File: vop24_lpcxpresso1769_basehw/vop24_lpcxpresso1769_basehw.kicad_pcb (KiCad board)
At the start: 2 copper layers, 113 parts, among them J1 Micro_SD_Card, J101 Conn_01x03_Male, J201 Screw_Terminal_01x02, J301 USB_B_Micro, J302 Conn_01x06_Male, J303 Conn_01x05_Male, J304 Screw_Terminal_01x02, J401 Conn_01x02, J402 Conn_01x02, J403 Conn_01x02, J404 Conn_01x04, J405 Conn_01x04, J406 Conn_01x04, U1 LPCXpresso1769, U101 MCP1700T-3302E_TT, U102 MCP1700T-3302E_TT, U103 TPS63001, U201 LM358, U301 TPD4S014, U302 LTC4411, U303 LT1512, U401 ADS1292, U402 LM334, U403 LM334, U404 LM334

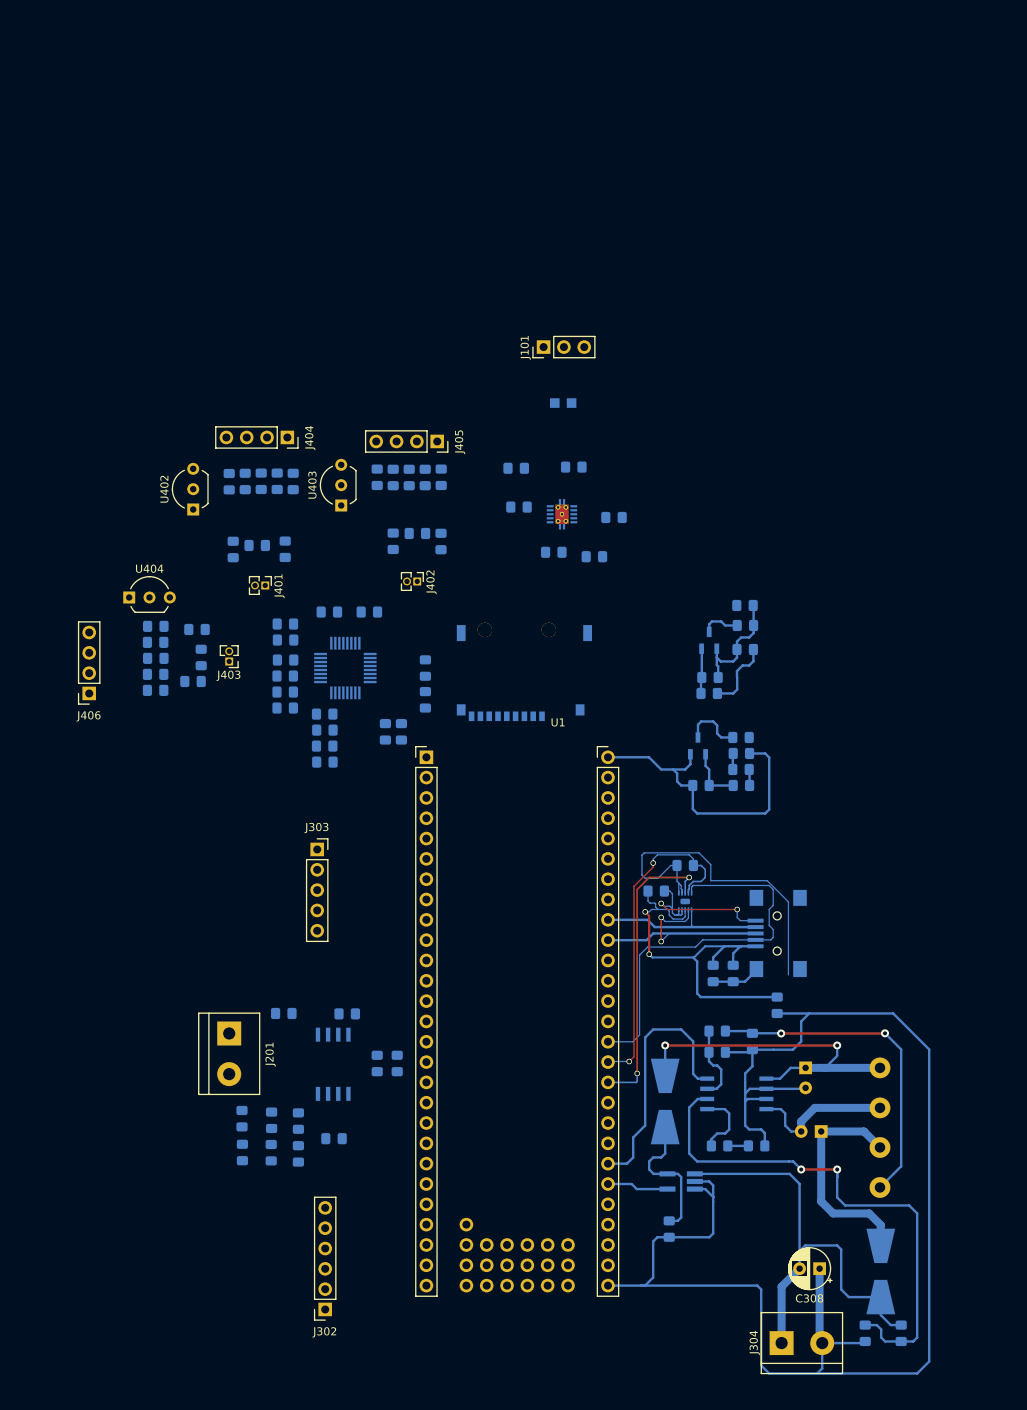
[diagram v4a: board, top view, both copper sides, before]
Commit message: PCB: ruteo de fuentes.    SCH: separacion de pistas de masa en fuentes
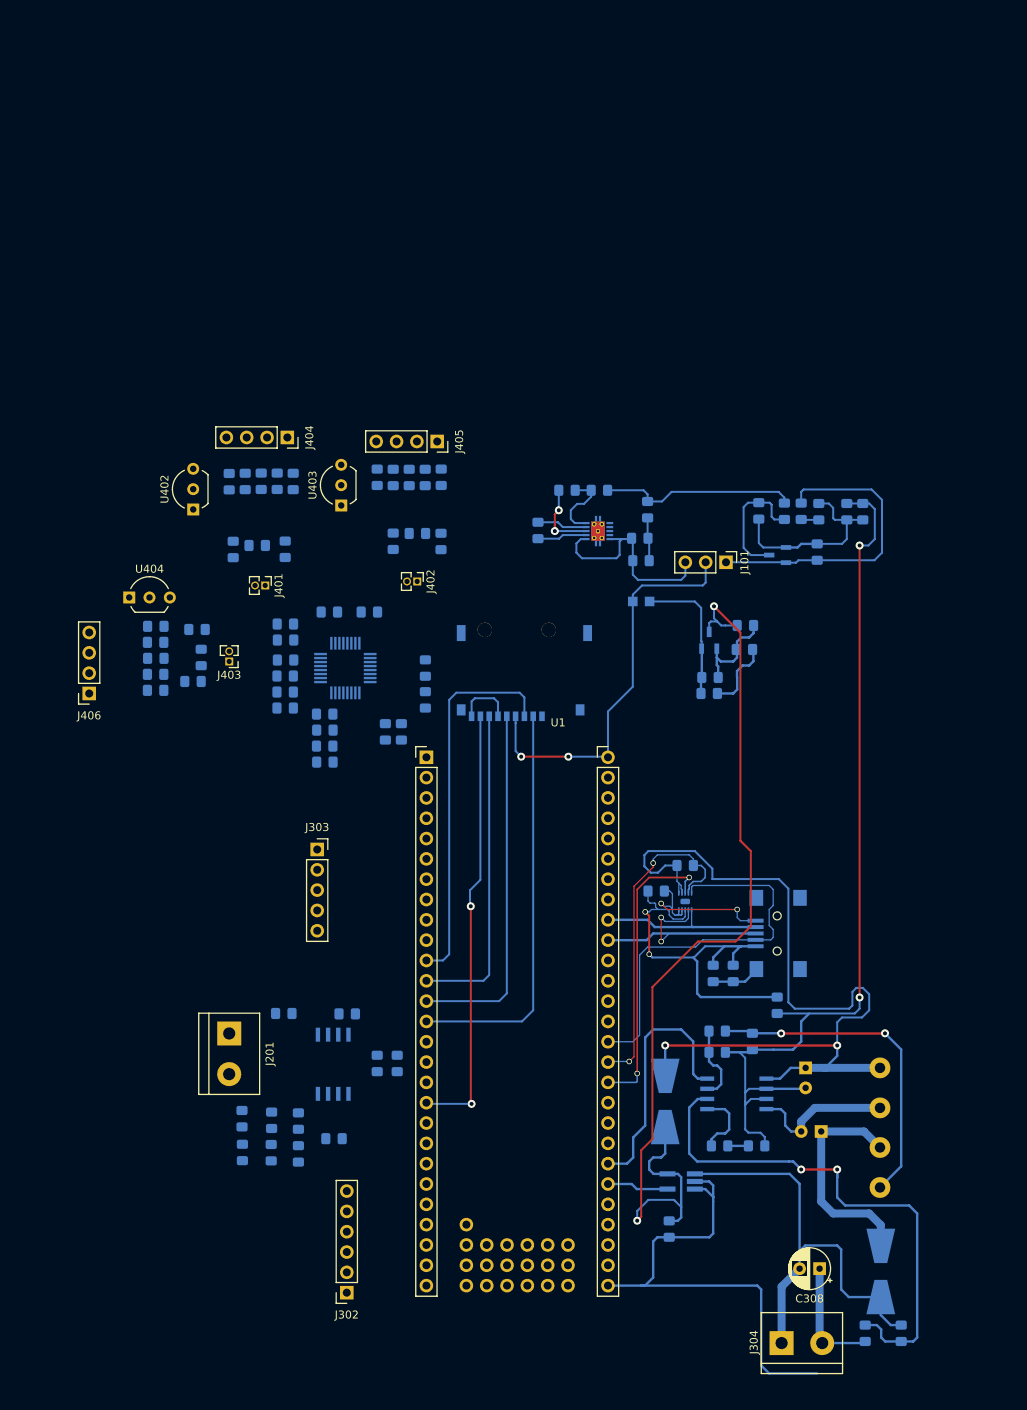
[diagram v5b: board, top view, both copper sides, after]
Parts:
- added R106: 1k, Resistor_SMD:R_0805_2012Metric_Pad1.15x1.40mm_HandSolder, B.Cu at (119.4, 92.0)
- R103: value 100 -> 0
- R104: value 1k -> 100
- moved R101 36.7 mm to (132.2, 74.8), turned to 90 degrees
- moved J101 35.3 mm to (117.1, 81.1), turned to 270 degrees
- moved R104 32.7 mm to (124.4, 74.7), turned to 90 degrees
- moved C105 32.6 mm to (128.5, 79.8), turned to 90 degrees
- moved D101 31.2 mm to (126.5, 74.7), turned to 90 degrees
- moved C101 28.4 mm to (121.2, 74.7), turned to 270 degrees
- moved FB101 26.6 mm to (106.5, 86.0), turned to 180 degrees
- moved U102 25.8 mm to (123.5, 80.2), turned to 180 degrees
- moved R105 19.5 mm to (128.7, 74.8), turned to 270 degrees
- moved R102 18.8 mm to (134.2, 74.8), turned to 90 degrees
- moved C104 12.9 mm to (107.3, 74.5), turned to 270 degrees
- moved R103 10.3 mm to (101.3, 72.1)
- moved L101 9.10 mm to (93.6, 77.1), turned to 270 degrees
- moved C103 6.92 mm to (97.2, 72.1), turned to 180 degrees
- moved C108 5.85 mm to (106.5, 80.9)
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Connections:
- C105 pad 1: /DVCC -> /fuentesLDO/DVCC_LDO
- C303 pad 2: /DGND -> /analogico/GNDBAT
- C304 pad 2: /DGND -> /analogico/GNDBAT
- C306 pad 2: /DGND -> /analogico/GNDBAT
- C308 pad 1: /DGND -> /analogico/GNDBAT
- D101 pad 2: /DVCC -> /fuentesLDO/DVCC_LDO
- J101 pad 1: /DVCC -> /fuentesLDO/DVCC_LDO
- J304 pad 2: /DGND -> /analogico/GNDBAT
- R101 pad 2: /DGND -> /analogico/GNDBAT
- R102 pad 1: /AGND -> /DGND
- R102 pad 2: /DGND -> /analogico/GNDBAT
- R103 pad 1: /fuentesLDO/VCC_NREG -> /AGND
- R103 pad 2: Net-(C104-Pad1) -> /analogico/GNDBAT
- R104 pad 1: /DGND -> /fuentesLDO/VCC_NREG
- R104 pad 2: Net-(D101-Pad1) -> Net-(C104-Pad1)
- R105 pad 1: /AGND -> /DGND
- R105 pad 2: Net-(D102-Pad1) -> Net-(D101-Pad1)
- R203 pad 1: /DGND -> /analogico/GNDBAT
- R303 pad 2: /DGND -> /analogico/GNDBAT
- R304 pad 2: /DGND -> /analogico/GNDBAT
- R306 pad 1: /DGND -> /analogico/GNDBAT
- R308 pad 1: /DGND -> /analogico/GNDBAT
- U102 pad 2: /DVCC -> /fuentesLDO/DVCC_LDO
- U302 pad 2: /DGND -> /analogico/GNDBAT
- U302 pad 3: /DGND -> /analogico/GNDBAT
- U303 pad 6: /DGND -> /analogico/GNDBAT
- U303 pad 7: /DGND -> /analogico/GNDBAT
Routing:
- net /analogico/GNDBAT: track 0.00 -> 131.9 mm, vias 0 -> 2
- net /fuentesLDO/VCC_NREG: track 30.2 -> 144.8 mm, vias 0 -> 2
- net /DGND: track 203.3 -> 108.0 mm, vias 0 -> 2
- net /CD_SD: track 0.00 -> 54.8 mm, vias 0 -> 2
- net /CS_SD: track 0.00 -> 50.7 mm
- net /MOSI_SD: track 0.00 -> 47.3 mm
- net /SCLK_SD: track 0.00 -> 45.1 mm
- net /MISO_SD: track 0.00 -> 40.5 mm
- net /fuentesLDO/DVCC_LDO: track 0.00 -> 38.9 mm
- net /fuentesLDO/DVCC_UD: track 0.00 -> 26.7 mm
- net /VUSB_OUT: track 87.4 -> 112.1 mm
- net Net-(C104-Pad1): track 0.00 -> 24.7 mm
- net /AVCC: track 5.65 -> 17.6 mm
- net /DVCC: track 38.4 -> 50.2 mm, vias 0 -> 2
- net Net-(L101-Pad1): track 0.00 -> 6.27 mm
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
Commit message: PCB: primera versión de ruteo finalizado sin poligonos. SCH: cambios de conexiones para facilitar conexiones
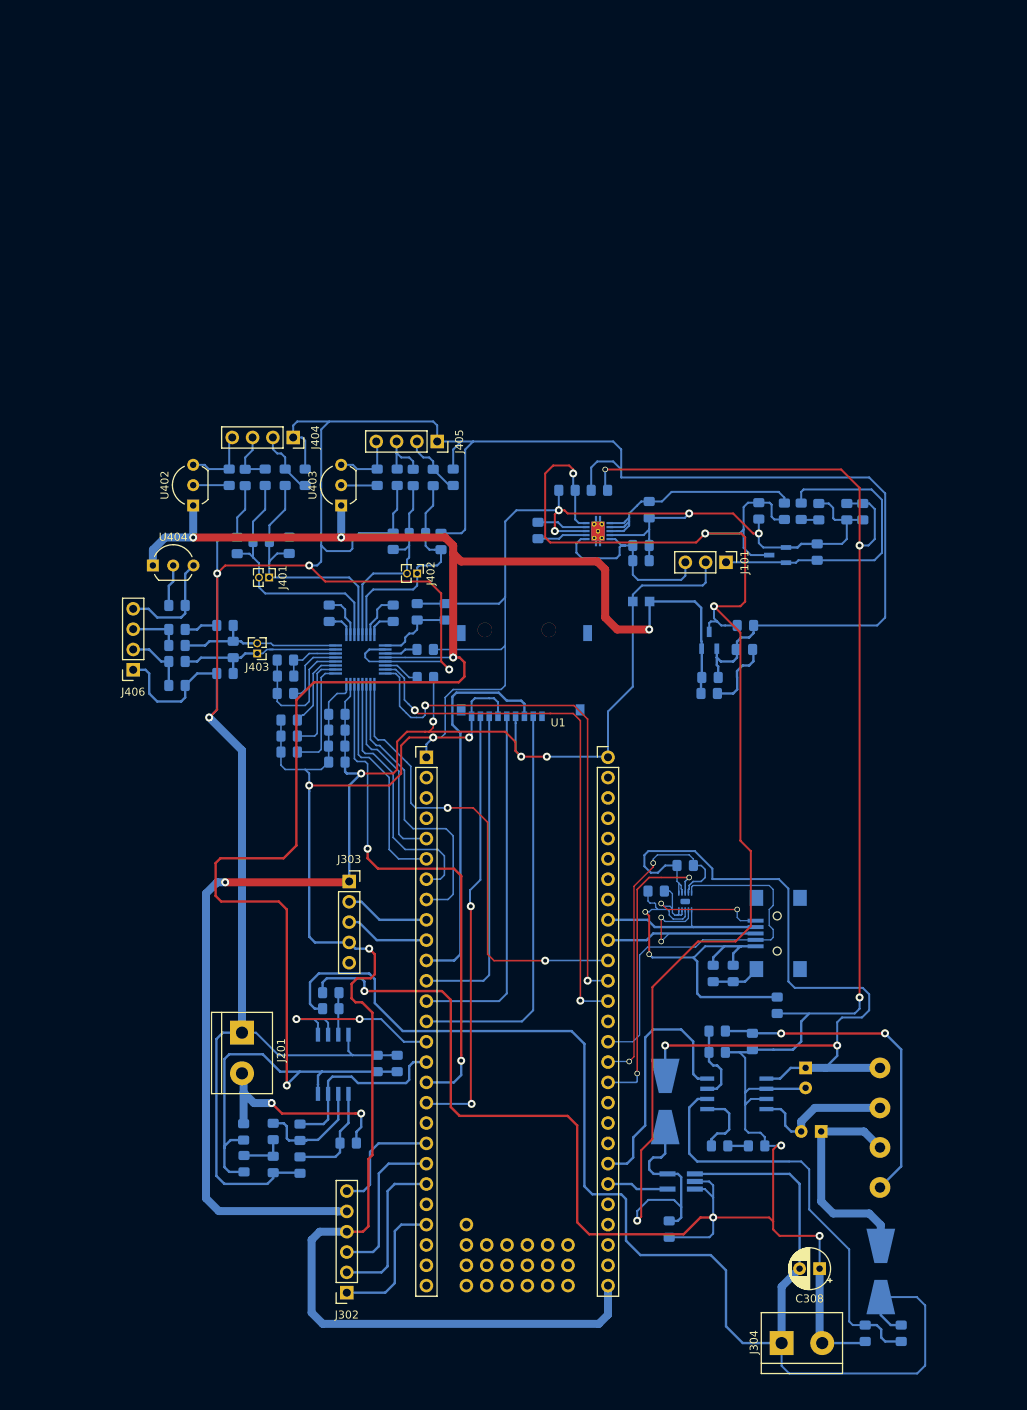
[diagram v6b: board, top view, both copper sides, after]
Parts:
- moved C403 16.0 mm to (82.0, 87.3)
- moved C404 15.5 mm to (78.5, 87.3)
- moved R203 6.42 mm to (67.7, 134.9)
- moved J406 6.25 mm to (43.0, 94.5)
- moved J303 5.66 mm to (70.0, 121.0)
- moved C402 5.52 mm to (62.5, 100.8)
- moved R403 5.52 mm to (62.5, 104.8)
- moved R405 5.52 mm to (62.5, 102.8)
- moved R412 5.50 mm to (83.0, 70.5)
- moved R418 5.00 mm to (80.5, 70.5)
- moved U404 4.98 mm to (45.5, 81.5)
- moved C409 4.50 mm to (62.0, 95.3)
- moved R402 4.50 mm to (62.0, 93.3)
- moved R420 4.49 mm to (48.5, 93.5), turned to 180 degrees
- moved R413 4.48 mm to (48.5, 89.5), turned to 180 degrees
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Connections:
- U1 pad 20: Net-(U1-Pad20) -> /BLE_EN
- U1 pad 23: /BLE_EN -> Net-(U1-Pad23)
- U1 pad 45: /CD_SD -> Net-(U1-Pad45)
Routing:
- net /AGND: track 12.1 -> 414.5 mm, vias 0 -> 4
- net /AVCC: track 17.6 -> 261.9 mm, vias 0 -> 5
- net /DGND: track 108.0 -> 326.4 mm, vias 2 -> 8
- net /analogico/GNDBAT: track 131.9 -> 302.8 mm, vias 2 -> 7
- net /DVCC: track 50.2 -> 185.7 mm, vias 2 -> 5
- net /analogico/VBAT: track 56.1 -> 177.5 mm
- net /PWDNE_ADS: track 0.00 -> 67.2 mm, vias 0 -> 2
- net /START_ADS: track 0.00 -> 67.1 mm, vias 0 -> 2
- net /DRDY_ADS: track 0.00 -> 65.3 mm, vias 0 -> 2
- net /CLK_ADS: track 0.00 -> 59.7 mm, vias 0 -> 2
- net /fuentesLDO/VCC_NREG: track 144.8 -> 198.9 mm, vias 2 -> 4
- net /CS_ADS: track 0.00 -> 36.8 mm
- net /SCLK_ADS: track 0.00 -> 33.5 mm
- net /ADS1292_esquematico/SENS1P: track 0.00 -> 33.4 mm
- net /ADS1292_esquematico/SENS1N: track 0.00 -> 32.6 mm
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
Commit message: PCB: ruteo finalizado con polígonos y texto en F.Cu. Agujeros en esquinas SCH: sin cambios
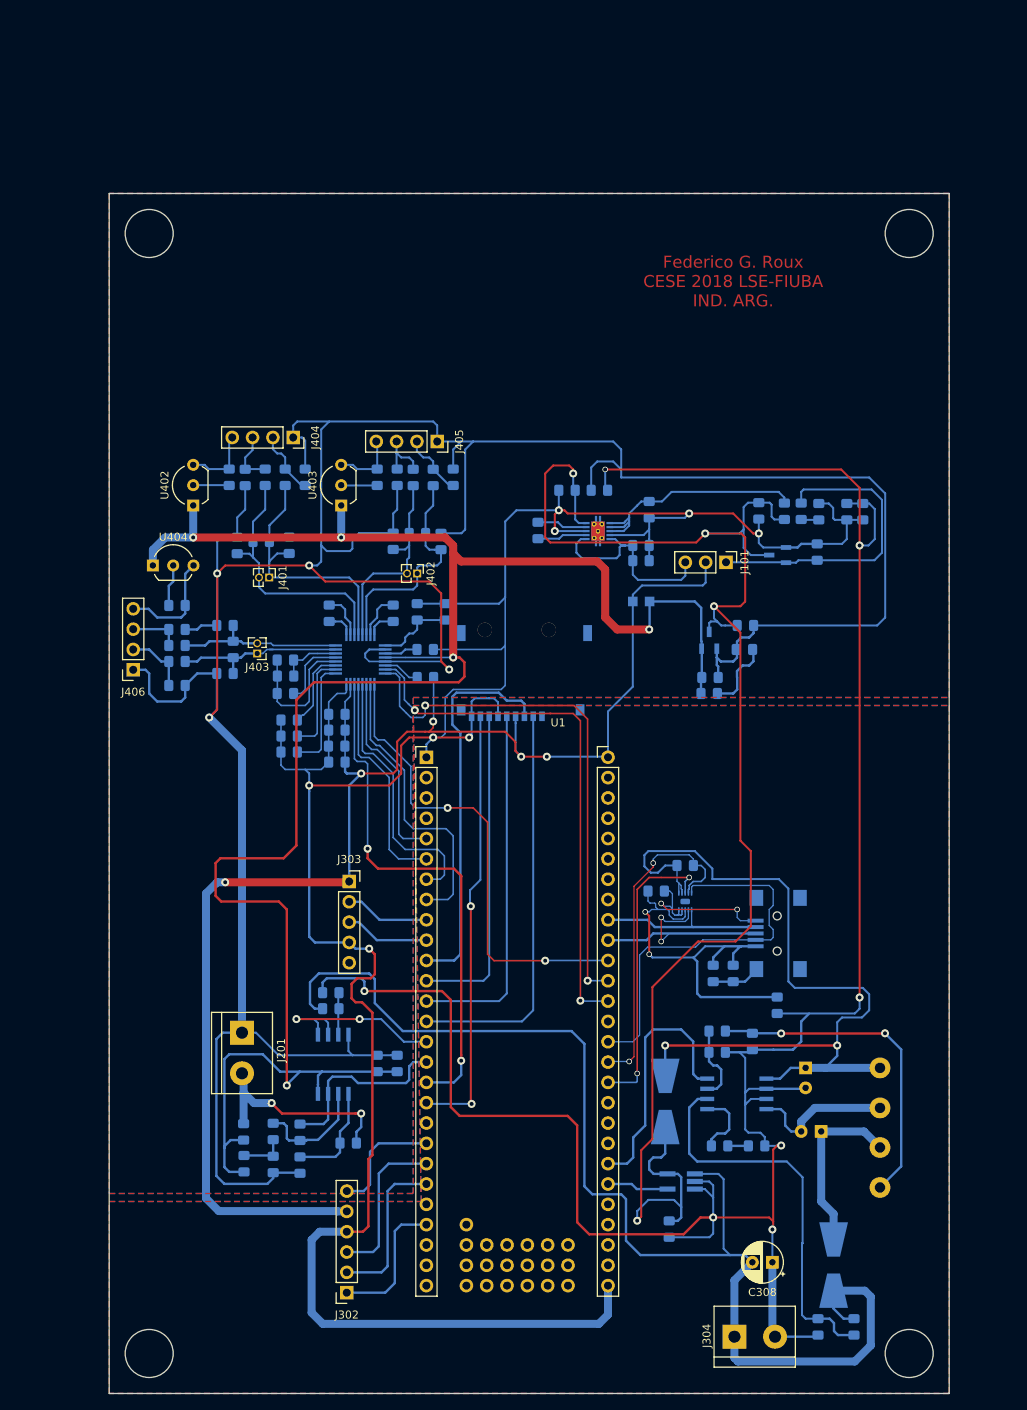
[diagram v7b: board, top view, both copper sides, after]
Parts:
- moved C308 5.95 mm to (122.9, 168.6)
- moved R307 5.95 mm to (133.1, 176.7)
- moved R308 5.95 mm to (128.6, 176.7)
- moved J304 5.95 mm to (118.2, 177.9)
- moved D302 5.95 mm to (130.6, 168.9)
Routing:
- net /analogico/VBAT: track 177.5 -> 151.5 mm
- net /analogico/GNDBAT: track 302.8 -> 296.6 mm
- net Net-(C307-Pad1): track 28.2 -> 22.3 mm
- net Net-(R307-Pad1): track 53.5 -> 49.3 mm
- added copper zone on B.Cu, net /AGND
- added copper zone on F.Cu, net /AGND
- added copper zone on B.Cu, net /DGND
- added copper zone on F.Cu, net /DGND
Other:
- board outline added: 105 x 150 mm
- board text added: "Federico G. Roux CESE 2018 LSE-FIUBA IND. ARG."

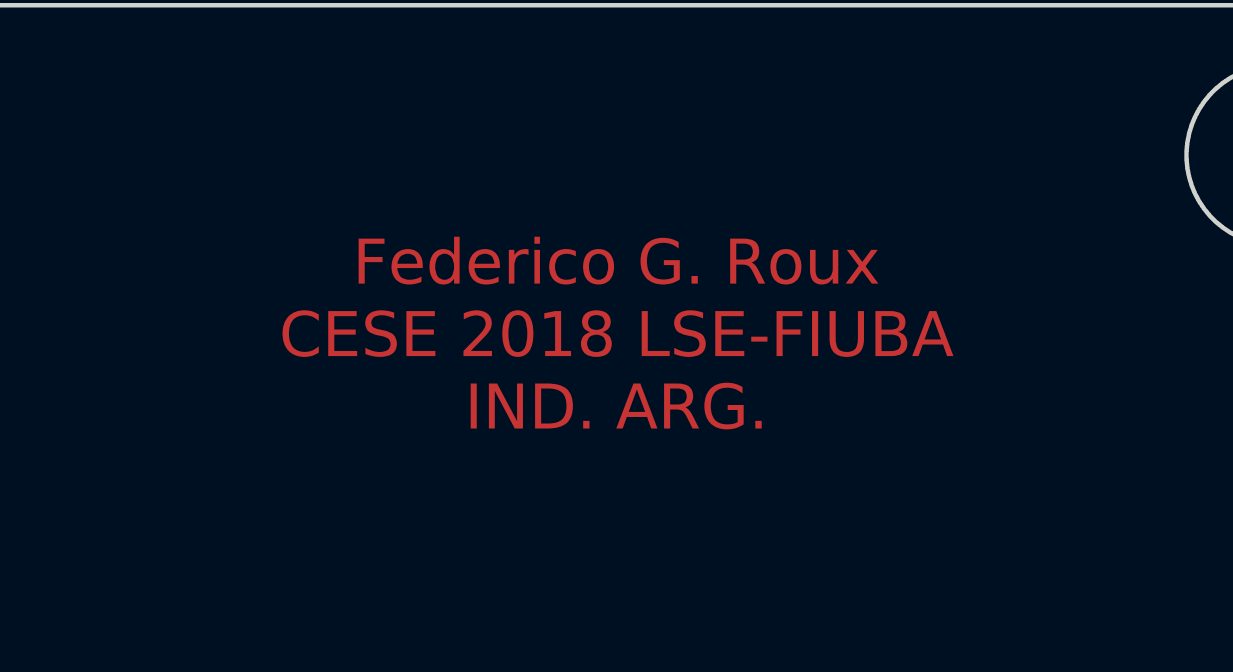
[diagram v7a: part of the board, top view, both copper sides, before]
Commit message: PCB: agregado de leyenda de nombre de placa y revisión
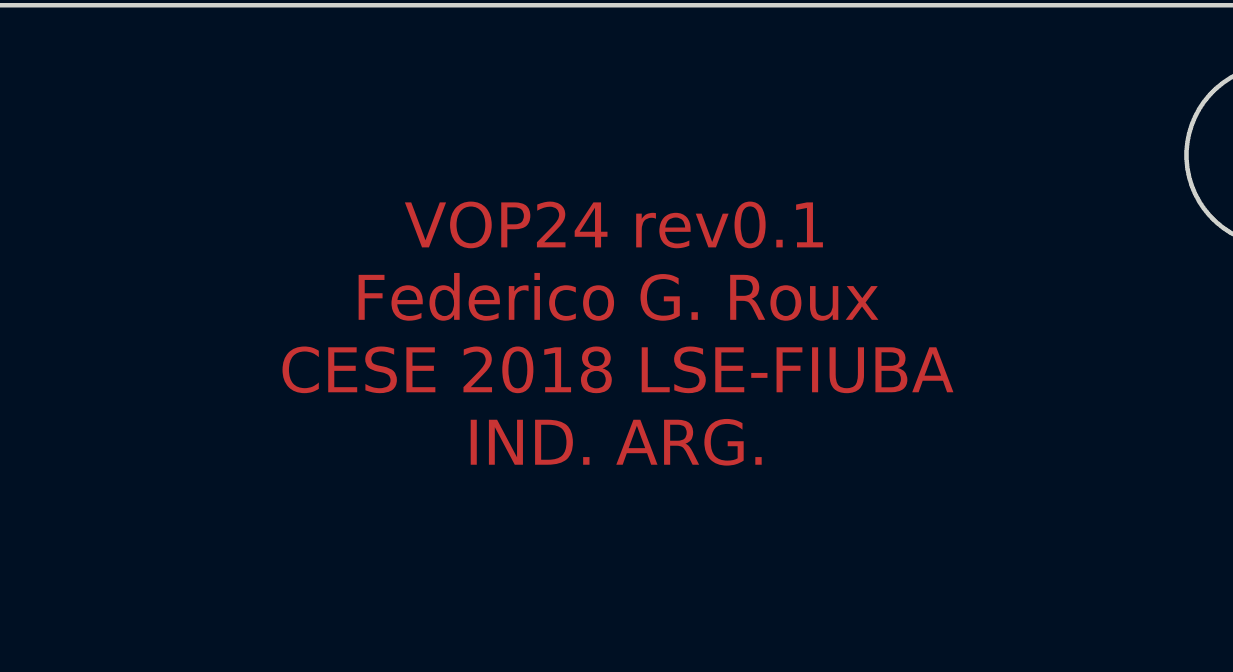
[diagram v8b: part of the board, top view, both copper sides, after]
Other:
- board text added: "VOP24 rev0.1 Federico G. Roux CESE 2018 LSE-FIUBA IND. ARG."
- board text removed: "Federico G. Roux CESE 2018 LSE-FIUBA IND. ARG."
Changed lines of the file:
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@@
     )
   )
-  (gr_text "Federico G. Roux\nCESE 2018 LSE-FIUBA\nIND. ARG." (at 118 46) (layer F.Cu)
+  (gr_text "VOP24 rev0.1\nFederico G. Roux\nCESE 2018 LSE-FIUBA\nIND. ARG." (at 118 46) (layer F.Cu)
     (effects (font (size 1.5 1.5) (thickness 0.3)))
   )
